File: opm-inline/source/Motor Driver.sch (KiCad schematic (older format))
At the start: 38 parts, among them IC1 TMC6200-TA, Q1 YJG95G06A, Q2 YJG95G06A, Q3 YJG95G06A, Q4 YJG95G06A, Q5 YJG95G06A, Q6 YJG95G06A

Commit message: fix connections
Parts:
- Q1, Q2, Q3, Q4, Q5, Q6: footprint Package_TO_SOT_SMD:TDSON-8-1 -> Libraries:PDFN-8
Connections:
- net labels added: DRV_EN, SPE, SPI1_MISO, SPI1_MOSI, SPI1_SCK, UH, UL, VH, VL, WH, WL, ~CS_DRIVER
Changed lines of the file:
@@
 F 0 "Q3" V 8031 5188 39  0000 R BNN
 F 1 "YJG95G06A" V 8031 5113 39  0000 C TNN
-F 2 "Package_TO_SOT_SMD:TDSON-8-1" H 7900 5075 39  0001 L CIN
+F 2 "Libraries:PDFN-8" H 7900 5075 39  0001 L CIN
 F 3 "" V 7700 5150 50  0001 L CNN
 	1    7700 5150
@@
 F 0 "Q4" V 8031 5988 39  0000 R BNN
 F 1 "YJG95G06A" V 8031 5913 39  0000 C TNN
-F 2 "Package_TO_SOT_SMD:TDSON-8-1" H 7900 5875 39  0001 L CIN
+F 2 "Libraries:PDFN-8" H 7900 5875 39  0001 L CIN
 F 3 "" V 7700 5950 50  0001 L CNN
 	1    7700 5950
@@
 F 0 "Q5" V 9681 3688 39  0000 R BNN
 F 1 "YJG95G06A" V 9681 3613 39  0000 C TNN
-F 2 "Package_TO_SOT_SMD:TDSON-8-1" H 9550 3575 39  0001 L CIN
+F 2 "Libraries:PDFN-8" H 9550 3575 39  0001 L CIN
 F 3 "" V 9350 3650 50  0001 L CNN
 	1    9350 3650
@@
 F 0 "Q6" V 9681 4488 39  0000 R BNN
 F 1 "YJG95G06A" V 9681 4413 39  0000 C TNN
-F 2 "Package_TO_SOT_SMD:TDSON-8-1" H 9550 4375 39  0001 L CIN
+F 2 "Libraries:PDFN-8" H 9550 4375 39  0001 L CIN
 F 3 "" V 9350 4450 50  0001 L CNN
 	1    9350 4450
@@
 F 0 "Q1" V 8031 2388 39  0000 R BNN
 F 1 "YJG95G06A" V 8031 2313 39  0000 C TNN
-F 2 "Package_TO_SOT_SMD:TDSON-8-1" H 7900 2275 39  0001 L CIN
+F 2 "Libraries:PDFN-8" H 7900 2275 39  0001 L CIN
 F 3 "" V 7700 2350 50  0001 L CNN
 	1    7700 2350
@@
 F 0 "Q2" V 8031 3188 39  0000 R BNN
 F 1 "YJG95G06A" V 8031 3113 39  0000 C TNN
-F 2 "Package_TO_SOT_SMD:TDSON-8-1" H 7900 3075 39  0001 L CIN
+F 2 "Libraries:PDFN-8" H 7900 3075 39  0001 L CIN
 F 3 "" V 7700 3150 50  0001 L CNN
 	1    7700 3150
@@
 	5200 3400 5200 3200
 Connection ~ 5200 3200
+Text HLabel 4300 4300 0    28   Input ~ 0
+UH
+Text HLabel 4300 4350 0    28   Input ~ 0
+UL
+Text HLabel 4300 4400 0    28   Input ~ 0
+VH
+Text HLabel 4300 4500 0    28   Input ~ 0
+WH
+Text HLabel 4300 4450 0    28   Input ~ 0
+VL
+Text HLabel 4300 4550 0    28   Input ~ 0
+WL
+Text HLabel 4300 4050 0    28   Input ~ 0
+~CS_DRIVER
+Text HLabel 4300 4100 0    28   Input ~ 0
+SPI1_SCK
+Text HLabel 4300 4150 0    28   Input ~ 0
+SPI1_MOSI
+Text HLabel 4300 4200 0    28   Input ~ 0
+SPI1_MISO
+Text HLabel 4300 3750 0    28   Input ~ 0
+DRV_EN
+Text HLabel 4300 3950 0    28   Input ~ 0
+SPE
 $EndSCHEMATC

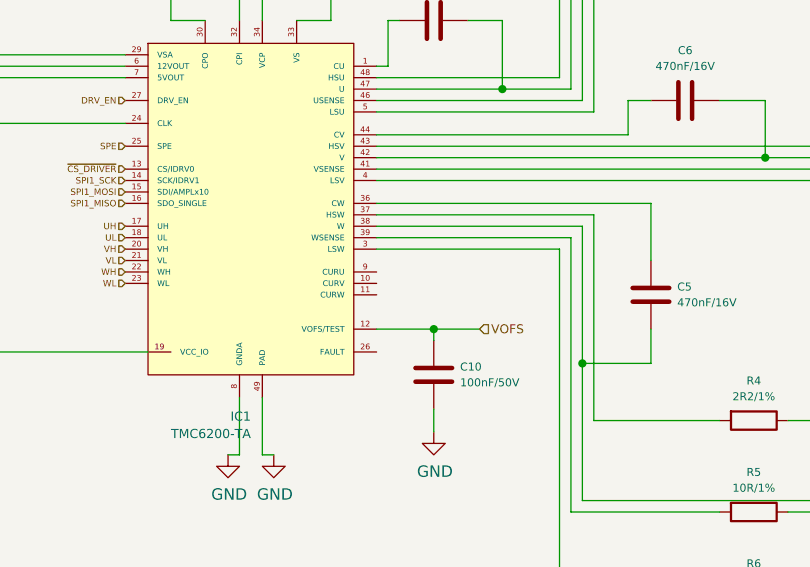
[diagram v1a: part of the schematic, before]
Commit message: adc out headers
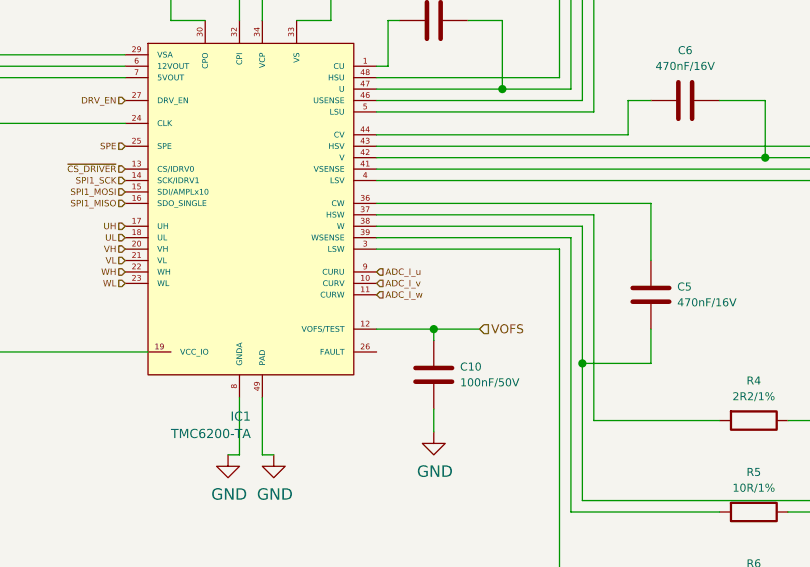
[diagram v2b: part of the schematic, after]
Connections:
- net labels added: ADC_I_u, ADC_I_v, ADC_I_w
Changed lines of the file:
@@
 Text HLabel 4300 3950 0    28   Input ~ 0
 SPE
+Text HLabel 5400 4500 2    28   Input ~ 0
+ADC_I_u
+Text HLabel 5400 4550 2    28   Input ~ 0
+ADC_I_v
+Text HLabel 5400 4600 2    28   Input ~ 0
+ADC_I_w
 $EndSCHEMATC

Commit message: add pcb
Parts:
- IC1: footprint Trinamic:QFN-44-1EP_7x7mm_P0.5mm_EP4x4mm -> Libraries:TMC6200-TA; symbol opm-inline-rescue:TMC6200-TA-opm-inline-cache -> opm-inline-rescue:TMC6200-TA-opm-inline-cache-opm-inline-rescue; Field5 (none) -> TMC6200-TA
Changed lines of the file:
@@
 	2950 3900 2950 3600
 $Comp
-L opm-inline-rescue:TMC6200-TA-opm-inline-cache IC?
+L opm-inline-rescue:TMC6200-TA-opm-inline-cache-opm-inline-rescue IC?
 U 1 1 61BC2F39
 P 4850 4200
@@
 F 0 "IC1" H 4850 3268 40  0000 R CNN
 F 1 "TMC6200-TA" H 4850 3192 40  0000 R CNN
-F 2 "Trinamic:QFN-44-1EP_7x7mm_P0.5mm_EP4x4mm" H 4850 3950 40  0001 C CNN
-F 3 "" H 4850 5025 40  0001 C CNN
+F 2 "Libraries:TMC6200-TA" H 4850 3950 40  0001 C CNN
+F 3 "https://trinamic.com/fileadmin/assets/Products/ICs_Documents/TMC6200_datasheet_Rev1.05.pdf" H 4850 5025 40  0001 C CNN
+F 4 "" H 4850 4200 50  0001 C CNN "LCSC"
+F 5 "TMC6200-TA" H 4850 4200 50  0001 C CNN "Field5"
 	1    4850 4200
 	1    0    0    -1

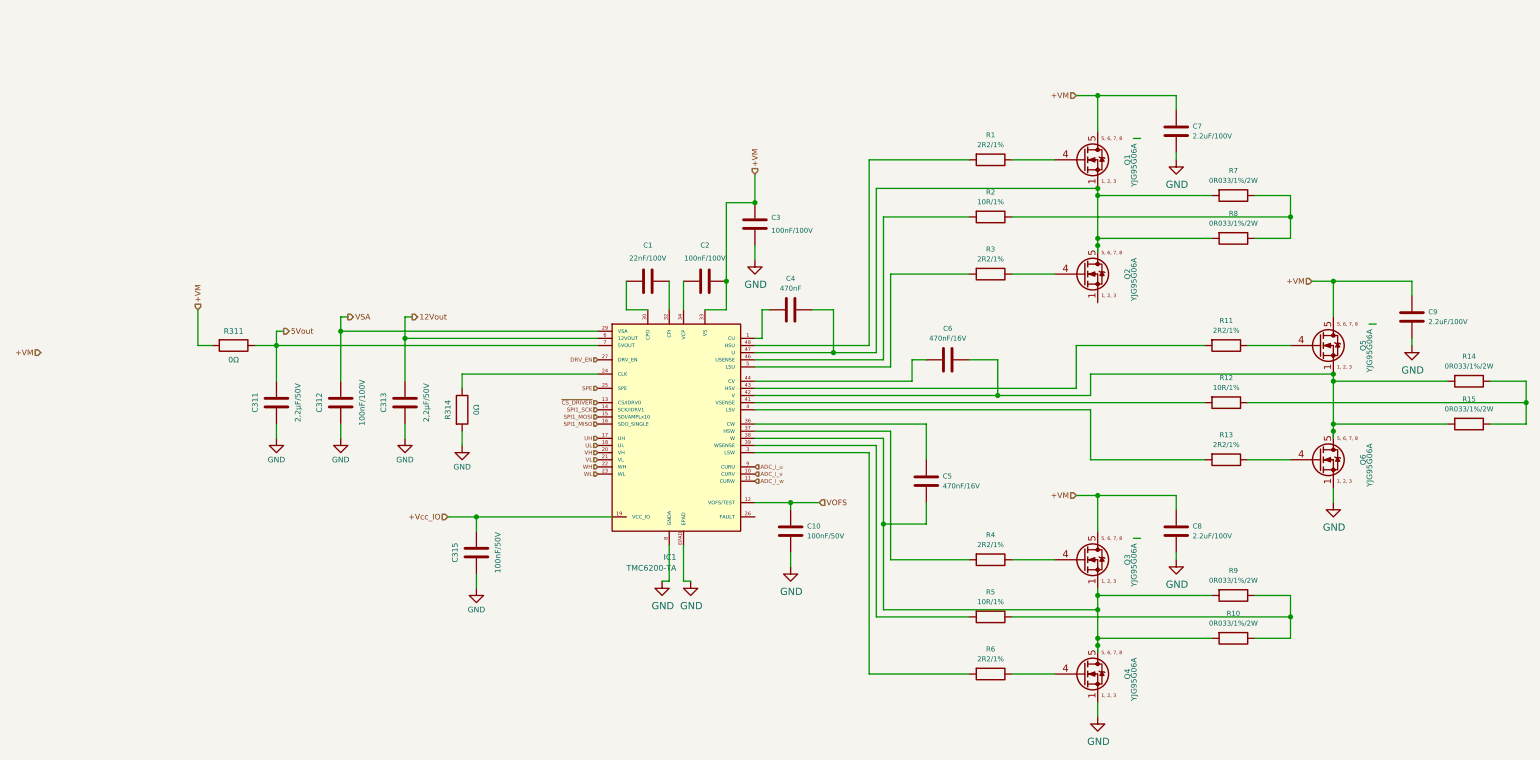
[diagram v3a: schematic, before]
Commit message: update resistors
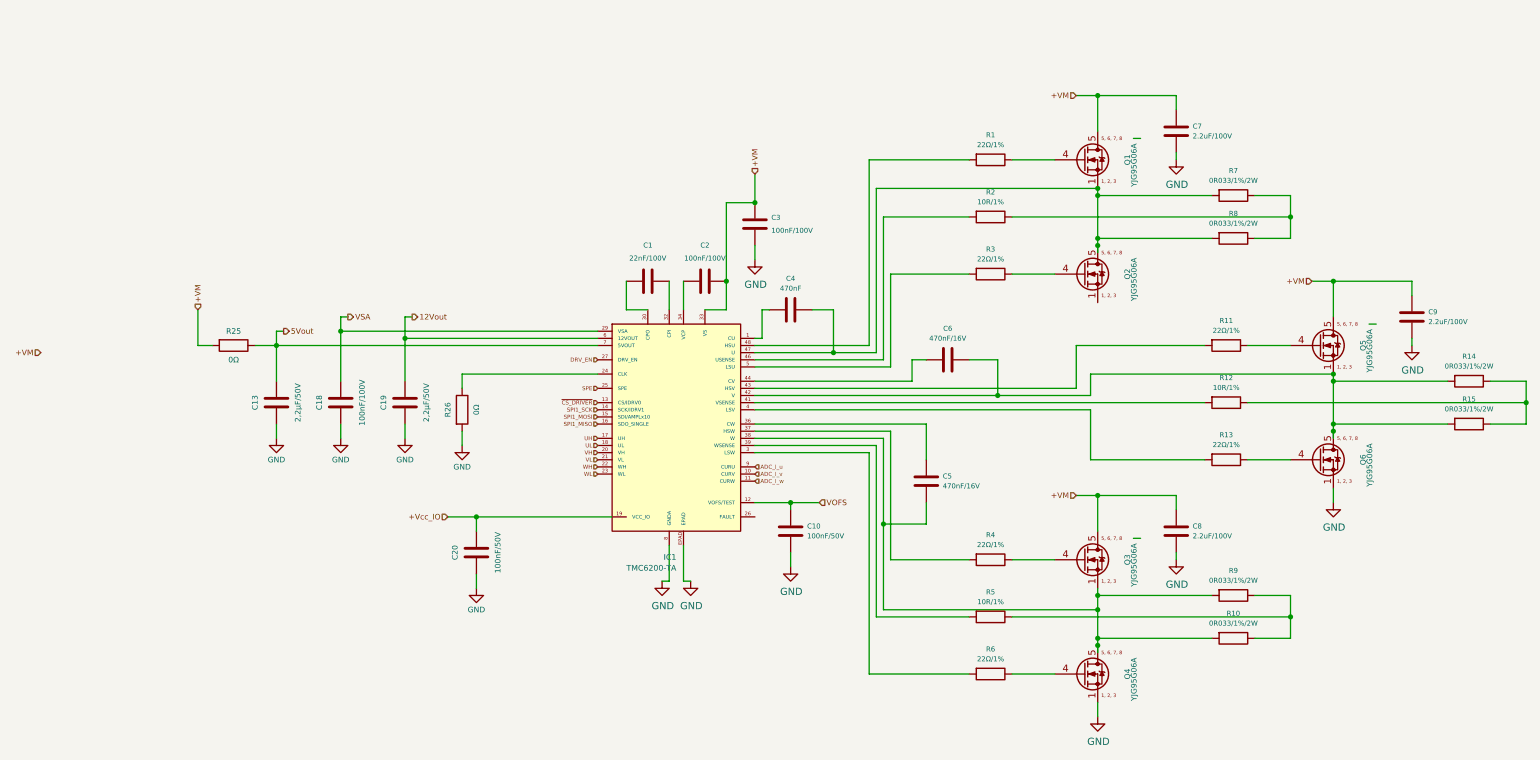
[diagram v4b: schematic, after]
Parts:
- R1, R11, R13, R3, R6: value 2R2/1% -> 22Ω/1%; LCSC C22977 -> C23345; alt RC0603FR-072R2L -> (none); manf_num 0603WAF200KT5E -> 0603WAF220JT5E
- R10, R14, R15, R7, R8, R9: footprint Resistor_SMD:R_0603_1608Metric -> Resistor_SMD:R_2512_6332Metric
- R4: value 2R2/1% -> 22Ω/1%; Field6 RC0603FR-072R2L -> (none); LCSC C22977 -> C23345; manf_num 0603WAF200KT5E -> 0603WAF220JT5E
- renumbered C311 to C13, C312 to C18, C313 to C19, C315 to C20, R311 to R25, R314 to R26
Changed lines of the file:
@@
 	3350 3850 3350 3950
 $Comp
-L Device:R R314
+L Device:R R26
 U 1 1 5DA1AADD
 P 3350 4100
-F 0 "R314" V 3250 4100 39  0000 C CNN
+F 0 "R26" V 3250 4100 39  0000 C CNN
 F 1 "0Ω" V 3450 4100 39  0000 C CNN
 F 2 "Resistor_SMD:R_0603_1608Metric" V 3280 4100 39  0001 C CNN
@@
 	3450 4850 3450 4950
 $Comp
-L Device:C C315
+L Device:C C20
 U 1 1 5DA56FA6
 P 3450 5100
-F 0 "C315" V 3300 5100 39  0000 C CNN
+F 0 "C20" V 3300 5100 39  0000 C CNN
 F 1 "100nF/50V" V 3600 5100 39  0000 C CNN
 F 2 "Capacitor_SMD:C_0603_1608Metric" H 3488 4950 39  0001 C CNN
@@
 +VM
 $Comp
-L Device:R R311
+L Device:R R25
 U 1 1 5DAB36B7
 P 1750 3650
-F 0 "R311" V 1650 3650 39  0000 C CNN
+F 0 "R25" V 1650 3650 39  0000 C CNN
 F 1 "0Ω" V 1850 3650 39  0000 C CNN
 F 2 "Resistor_SMD:R_0603_1608Metric" V 1680 3650 39  0001 C CNN
@@
 	1900 3650 2050 3650
 $Comp
-L Device:C C311
+L Device:C C13
 U 1 1 5DADB8FC
 P 2050 4050
-F 0 "C311" V 1900 4050 39  0000 C CNN
+F 0 "C13" V 1900 4050 39  0000 C CNN
 F 1 "2,2μF/50V" V 2200 4050 39  0000 C CNN
 F 2 "Capacitor_SMD:C_0805_2012Metric" H 2088 3900 39  0001 C CNN
@@
 	2050 4300 2050 4200
 $Comp
-L Device:C C312
+L Device:C C18
 U 1 1 5DB0D3D6
 P 2500 4050
-F 0 "C312" V 2350 4050 39  0000 C CNN
+F 0 "C18" V 2350 4050 39  0000 C CNN
 F 1 "100nF/100V" V 2650 4050 39  0000 C CNN
 F 2 "Capacitor_SMD:C_0805_2012Metric" H 2538 3900 39  0001 C CNN
@@
 $EndComp
 $Comp
-L Device:C C313
+L Device:C C19
 U 1 1 5DB0D99C
 P 2950 4050
-F 0 "C313" V 2800 4050 39  0000 C CNN
+F 0 "C19" V 2800 4050 39  0000 C CNN
 F 1 "2,2μF/50V" V 3100 4050 39  0000 C CNN
 F 2 "Capacitor_SMD:C_0805_2012Metric" H 2988 3900 39  0001 C CNN
@@
 P 7050 5150
 F 0 "R4" V 6876 5150 35  0000 C CNN
-F 1 "2R2/1%" V 6945 5150 35  0000 C CNN
+F 1 "22Ω/1%" V 6945 5150 35  0000 C CNN
 F 2 "Resistor_SMD:R_0603_1608Metric" V 6980 5150 50  0001 C CNN
-F 3 "https://datasheet.lcsc.com/lcsc/2110252130_UNI-ROYAL-Uniroyal-Elec-0603WAF200KT5E_C22977.pdf" H 7050 5150 50  0001 C CNN
-F 4 "C22977" V 7050 5150 50  0001 C CNN "LCSC"
-F 5 "0603WAF200KT5E" V 7050 5150 50  0001 C CNN "manf_num"
-F 6 "RC0603FR-072R2L" V 7050 5150 50  0001 C CNN "Field6"
+F 3 "https://datasheet.lcsc.com/szlcsc/Uniroyal-Elec-0603WAF220JT5E_C23345.pdf" H 7050 5150 50  0001 C CNN
+F 4 "C23345" V 7050 5150 50  0001 C CNN "LCSC"
+F 5 "0603WAF220JT5E" V 7050 5150 50  0001 C CNN "manf_num"
+F 6 "" V 7050 5150 50  0001 C CNN "alt"
 	1    7050 5150
 	0    1    1    0
@@
 P 7050 5950
 F 0 "R6" V 6876 5950 35  0000 C CNN
-F 1 "2R2/1%" V 6945 5950 35  0000 C CNN
+F 1 "22Ω/1%" V 6945 5950 35  0000 C CNN
 F 2 "Resistor_SMD:R_0603_1608Metric" V 6980 5950 50  0001 C CNN
-F 3 "https://datasheet.lcsc.com/lcsc/2110252130_UNI-ROYAL-Uniroyal-Elec-0603WAF200KT5E_C22977.pdf" H 7050 5950 50  0001 C CNN
-F 4 "C22977" V 7050 5950 50  0001 C CNN "LCSC"
-F 5 "0603WAF200KT5E" V 7050 5950 50  0001 C CNN "manf_num"
-F 6 "RC0603FR-072R2L" V 7050 5950 50  0001 C CNN "alt"
+F 3 "https://datasheet.lcsc.com/szlcsc/Uniroyal-Elec-0603WAF220JT5E_C23345.pdf" H 7050 5950 50  0001 C CNN
+F 4 "C23345" V 7050 5950 50  0001 C CNN "LCSC"
+F 5 "0603WAF220JT5E" V 7050 5950 50  0001 C CNN "manf_num"
+F 6 "" V 7050 5950 50  0001 C CNN "alt"
 	1    7050 5950
 	0    1    1    0
@@
 F 0 "R9" V 8576 5400 35  0000 C CNN
 F 1 "0R033/1%/2W" V 8645 5400 35  0000 C CNN
-F 2 "Resistor_SMD:R_0603_1608Metric" V 8680 5400 50  0001 C CNN
+F 2 "Resistor_SMD:R_2512_6332Metric" V 8680 5400 50  0001 C CNN
 F 3 "https://datasheet.lcsc.com/lcsc/2108141930_prosemi-LMP25NF2P0R033_C2838960.pdf" H 8750 5400 50  0001 C CNN
 F 4 "C2838960" V 8750 5400 50  0001 C CNN "LCSC"
@@
 F 0 "R10" V 8576 5700 35  0000 C CNN
 F 1 "0R033/1%/2W" V 8645 5700 35  0000 C CNN
-F 2 "Resistor_SMD:R_0603_1608Metric" V 8680 5700 50  0001 C CNN
+F 2 "Resistor_SMD:R_2512_6332Metric" V 8680 5700 50  0001 C CNN
 F 3 "https://datasheet.lcsc.com/lcsc/2108141930_prosemi-LMP25NF2P0R033_C2838960.pdf" H 8750 5700 50  0001 C CNN
 F 4 "C2838960" V 8750 5700 50  0001 C CNN "LCSC"
@@
 P 8700 3650
 F 0 "R11" V 8526 3650 35  0000 C CNN
-F 1 "2R2/1%" V 8595 3650 35  0000 C CNN
+F 1 "22Ω/1%" V 8595 3650 35  0000 C CNN
 F 2 "Resistor_SMD:R_0603_1608Metric" V 8630 3650 50  0001 C CNN
-F 3 "https://datasheet.lcsc.com/lcsc/2110252130_UNI-ROYAL-Uniroyal-Elec-0603WAF200KT5E_C22977.pdf" H 8700 3650 50  0001 C CNN
-F 4 "C22977" V 8700 3650 50  0001 C CNN "LCSC"
-F 5 "0603WAF200KT5E" V 8700 3650 50  0001 C CNN "manf_num"
-F 6 "RC0603FR-072R2L" V 8700 3650 50  0001 C CNN "alt"
+F 3 "https://datasheet.lcsc.com/szlcsc/Uniroyal-Elec-0603WAF220JT5E_C23345.pdf" H 8700 3650 50  0001 C CNN
+F 4 "C23345" V 8700 3650 50  0001 C CNN "LCSC"
+F 5 "0603WAF220JT5E" V 8700 3650 50  0001 C CNN "manf_num"
+F 6 "" V 8700 3650 50  0001 C CNN "alt"
 	1    8700 3650
 	0    1    1    0
@@
 P 8700 4450
 F 0 "R13" V 8526 4450 35  0000 C CNN
-F 1 "2R2/1%" V 8595 4450 35  0000 C CNN
+F 1 "22Ω/1%" V 8595 4450 35  0000 C CNN
 F 2 "Resistor_SMD:R_0603_1608Metric" V 8630 4450 50  0001 C CNN
-F 3 "https://datasheet.lcsc.com/lcsc/2110252130_UNI-ROYAL-Uniroyal-Elec-0603WAF200KT5E_C22977.pdf" H 8700 4450 50  0001 C CNN
-F 4 "C22977" V 8700 4450 50  0001 C CNN "LCSC"
-F 5 "0603WAF200KT5E" V 8700 4450 50  0001 C CNN "manf_num"
-F 6 "RC0603FR-072R2L" V 8700 4450 50  0001 C CNN "alt"
+F 3 "https://datasheet.lcsc.com/szlcsc/Uniroyal-Elec-0603WAF220JT5E_C23345.pdf" H 8700 4450 50  0001 C CNN
+F 4 "C23345" V 8700 4450 50  0001 C CNN "LCSC"
+F 5 "0603WAF220JT5E" V 8700 4450 50  0001 C CNN "manf_num"
+F 6 "" V 8700 4450 50  0001 C CNN "alt"
 	1    8700 4450
 	0    1    1    0
@@
 F 0 "R14" V 10226 3900 35  0000 C CNN
 F 1 "0R033/1%/2W" V 10295 3900 35  0000 C CNN
-F 2 "Resistor_SMD:R_0603_1608Metric" V 10330 3900 50  0001 C CNN
+F 2 "Resistor_SMD:R_2512_6332Metric" V 10330 3900 50  0001 C CNN
 F 3 "https://datasheet.lcsc.com/lcsc/2108141930_prosemi-LMP25NF2P0R033_C2838960.pdf" H 10400 3900 50  0001 C CNN
 F 4 "C2838960" V 10400 3900 50  0001 C CNN "LCSC"
@@
 F 0 "R15" V 10226 4200 35  0000 C CNN
 F 1 "0R033/1%/2W" V 10295 4200 35  0000 C CNN
-F 2 "Resistor_SMD:R_0603_1608Metric" V 10330 4200 50  0001 C CNN
+F 2 "Resistor_SMD:R_2512_6332Metric" V 10330 4200 50  0001 C CNN
 F 3 "https://datasheet.lcsc.com/lcsc/2108141930_prosemi-LMP25NF2P0R033_C2838960.pdf" H 10400 4200 50  0001 C CNN
 F 4 "C2838960" V 10400 4200 50  0001 C CNN "LCSC"
@@
 P 7050 2350
 F 0 "R1" V 6876 2350 35  0000 C CNN
-F 1 "2R2/1%" V 6945 2350 35  0000 C CNN
+F 1 "22Ω/1%" V 6945 2350 35  0000 C CNN
 F 2 "Resistor_SMD:R_0603_1608Metric" V 6980 2350 50  0001 C CNN
-F 3 "https://datasheet.lcsc.com/lcsc/2110252130_UNI-ROYAL-Uniroyal-Elec-0603WAF200KT5E_C22977.pdf" H 7050 2350 50  0001 C CNN
-F 4 "C22977" V 7050 2350 50  0001 C CNN "LCSC"
-F 5 "0603WAF200KT5E" V 7050 2350 50  0001 C CNN "manf_num"
-F 6 "RC0603FR-072R2L" V 7050 2350 50  0001 C CNN "alt"
+F 3 "https://datasheet.lcsc.com/szlcsc/Uniroyal-Elec-0603WAF220JT5E_C23345.pdf" H 7050 2350 50  0001 C CNN
+F 4 "C23345" V 7050 2350 50  0001 C CNN "LCSC"
+F 5 "0603WAF220JT5E" V 7050 2350 50  0001 C CNN "manf_num"
+F 6 "" V 7050 2350 50  0001 C CNN "alt"
 	1    7050 2350
 	0    1    1    0
@@
 P 7050 3150
 F 0 "R3" V 6876 3150 35  0000 C CNN
-F 1 "2R2/1%" V 6945 3150 35  0000 C CNN
+F 1 "22Ω/1%" V 6945 3150 35  0000 C CNN
 F 2 "Resistor_SMD:R_0603_1608Metric" V 6980 3150 50  0001 C CNN
-F 3 "https://datasheet.lcsc.com/lcsc/2110252130_UNI-ROYAL-Uniroyal-Elec-0603WAF200KT5E_C22977.pdf" H 7050 3150 50  0001 C CNN
-F 4 "C22977" V 7050 3150 50  0001 C CNN "LCSC"
-F 5 "0603WAF200KT5E" V 7050 3150 50  0001 C CNN "manf_num"
-F 6 "RC0603FR-072R2L" V 7050 3150 50  0001 C CNN "alt"
+F 3 "https://datasheet.lcsc.com/szlcsc/Uniroyal-Elec-0603WAF220JT5E_C23345.pdf" H 7050 3150 50  0001 C CNN
+F 4 "C23345" V 7050 3150 50  0001 C CNN "LCSC"
+F 5 "0603WAF220JT5E" V 7050 3150 50  0001 C CNN "manf_num"
+F 6 "" V 7050 3150 50  0001 C CNN "alt"
 	1    7050 3150
 	0    1    1    0
@@
 F 0 "R7" V 8576 2600 35  0000 C CNN
 F 1 "0R033/1%/2W" V 8645 2600 35  0000 C CNN
-F 2 "Resistor_SMD:R_0603_1608Metric" V 8680 2600 50  0001 C CNN
+F 2 "Resistor_SMD:R_2512_6332Metric" V 8680 2600 50  0001 C CNN
 F 3 "https://datasheet.lcsc.com/lcsc/2108141930_prosemi-LMP25NF2P0R033_C2838960.pdf" H 8750 2600 50  0001 C CNN
 F 4 "C2838960" V 8750 2600 50  0001 C CNN "LCSC"
@@
 F 0 "R8" V 8576 2900 35  0000 C CNN
 F 1 "0R033/1%/2W" V 8645 2900 35  0000 C CNN
-F 2 "Resistor_SMD:R_0603_1608Metric" V 8680 2900 50  0001 C CNN
+F 2 "Resistor_SMD:R_2512_6332Metric" V 8680 2900 50  0001 C CNN
 F 3 "https://datasheet.lcsc.com/lcsc/2108141930_prosemi-LMP25NF2P0R033_C2838960.pdf" H 8750 2900 50  0001 C CNN
 F 4 "C2838960" V 8750 2900 50  0001 C CNN "LCSC"
